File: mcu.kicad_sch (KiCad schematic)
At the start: 30 parts, among them J7 CONN_MCU_SERIAL, SW1 SW_RST, SW2 SW_BOOT0, U2 STM32F765IITx, Y2 25MHz

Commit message: Final annotate pass
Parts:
- gave numbers to parts that had none: 1
- renumbered C9 to C301, C10 to C302, C11 to C303, C12 to C304, C13 to C305, C14 to C306, C15 to C307, C16 to C308, C17 to C309, C18 to C310, C19 to C311, C20 to C312, C21 to C313, C22 to C314, C23 to C315, C24 to C316, C25 to C317, C26 to C318, C27 to C319, C28 to C320, J7 to J301, R12 to R301, R13 to R302, R14 to R303, R15 to R304, SW1 to SW301, SW2 to SW302, U2 to U301, Y2 to Y301

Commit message: Re-annotation, footprints
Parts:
- J301: footprint (none) -> Connector_PinSocket_2.54mm:PinSocket_1x05_P2.54mm_Vertical
- J302: footprint (none) -> Connector_PinSocket_2.54mm:PinSocket_1x13_P2.54mm_Vertical
- R301, R302, R303, R304: footprint (none) -> Resistor_SMD:R_0603_1608Metric_Pad0.98x0.95mm_HandSolder
- Y301: footprint Crystal:Crystal_SMD_5032-4Pin_5.0x3.2mm -> Crystal:Crystal_SMD_5032-2Pin_5.0x3.2mm_HandSoldering
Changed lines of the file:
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@@
       (effects (font (size 1.27 1.27)) (justify left))
     )
-    (property "Footprint" "" (id 2) (at 139.192 157.48 90)
+    (property "Footprint" "Resistor_SMD:R_0603_1608Metric_Pad0.98x0.95mm_HandSolder" (id 2) (at 139.192 157.48 90)
       (effects (font (size 1.27 1.27)) hide)
     )
@@
     (property "Reference" "R301" (id 0) (at 39.37 134.62 90))
     (property "Value" "10k" (id 1) (at 39.37 132.4411 90))
-    (property "Footprint" "" (id 2) (at 39.37 136.398 90)
+    (property "Footprint" "Resistor_SMD:R_0603_1608Metric_Pad0.98x0.95mm_HandSolder" (id 2) (at 39.37 136.398 90)
       (effects (font (size 1.27 1.27)) hide)
     )
@@
     (property "Reference" "R303" (id 0) (at 39.37 144.78 90))
     (property "Value" "10k" (id 1) (at 39.37 142.6011 90))
-    (property "Footprint" "" (id 2) (at 39.37 146.558 90)
+    (property "Footprint" "Resistor_SMD:R_0603_1608Metric_Pad0.98x0.95mm_HandSolder" (id 2) (at 39.37 146.558 90)
       (effects (font (size 1.27 1.27)) hide)
     )
@@
     (property "Reference" "R302" (id 0) (at 39.37 139.7 90))
     (property "Value" "10k" (id 1) (at 39.37 137.5211 90))
-    (property "Footprint" "" (id 2) (at 39.37 141.478 90)
+    (property "Footprint" "Resistor_SMD:R_0603_1608Metric_Pad0.98x0.95mm_HandSolder" (id 2) (at 39.37 141.478 90)
       (effects (font (size 1.27 1.27)) hide)
     )
@@
     (property "Reference" "J302" (id 0) (at 210.82 146.211 90))
     (property "Value" "Conn_01x13_Female" (id 1) (at 210.82 148.7479 90))
-    (property "Footprint" "" (id 2) (at 210.82 149.86 0)
+    (property "Footprint" "Connector_PinSocket_2.54mm:PinSocket_1x13_P2.54mm_Vertical" (id 2) (at 210.82 149.86 0)
       (effects (font (size 1.27 1.27)) hide)
     )
@@
       (effects (font (size 1.27 1.27)) (justify left))
     )
-    (property "Footprint" "Crystal:Crystal_SMD_5032-4Pin_5.0x3.2mm" (id 2) (at 139.7 171.45 0)
+    (property "Footprint" "Crystal:Crystal_SMD_5032-2Pin_5.0x3.2mm_HandSoldering" (id 2) (at 139.7 171.45 0)
       (effects (font (size 1.27 1.27)) hide)
     )
@@
     (property "Reference" "J301" (id 0) (at 104.14 155.101 90))
     (property "Value" "CONN_MCU_SERIAL" (id 1) (at 104.14 157.6379 90))
-    (property "Footprint" "" (id 2) (at 105.41 158.75 0)
-      (effects (font (size 1.27 1.27)) hide)
-    )
+    (property "Footprint" "Connector_PinSocket_2.54mm:PinSocket_1x05_P2.54mm_Vertical" (id 2) (at 105.41 158.75 0)
+      (effects (font (size 1.27 1.27)) hide)
+    )

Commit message: Add button footprint
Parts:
- SW301, SW302: footprint (none) -> marco-ram-board:DTSMW69N
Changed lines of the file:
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@@
       (effects (font (size 1.27 1.27)) (justify right))
     )
-    (property "Footprint" "" (id 2) (at 57.15 157.48 0)
+    (property "Footprint" "marco-ram-board:DTSMW69N" (id 2) (at 57.15 157.48 0)
       (effects (font (size 1.27 1.27)) hide)
     )
@@
       (effects (font (size 1.27 1.27)) (justify right))
     )
-    (property "Footprint" "" (id 2) (at 46.99 161.29 0)
-      (effects (font (size 1.27 1.27)) hide)
-    )
+    (property "Footprint" "marco-ram-board:DTSMW69N" (id 2) (at 46.99 161.29 0)
+      (effects (font (size 1.27 1.27)) hide)
+    )

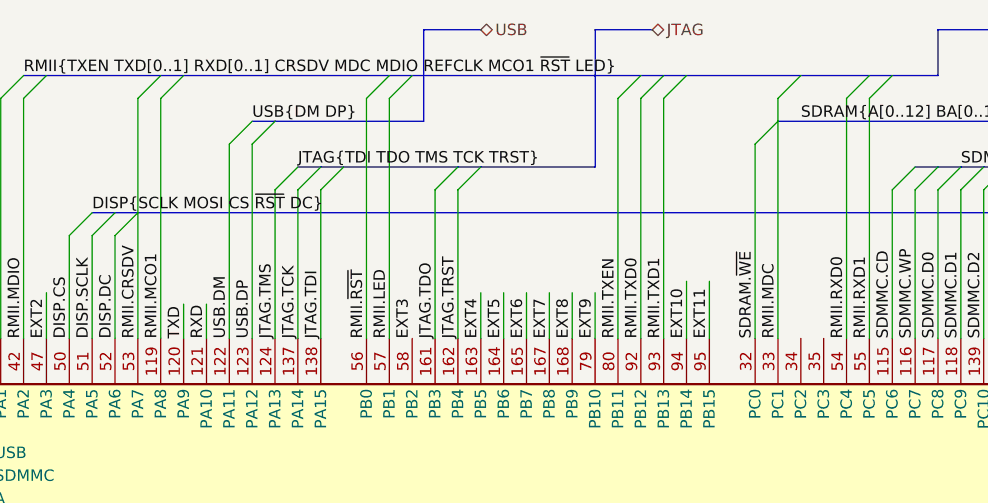
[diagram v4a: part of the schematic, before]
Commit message: Also connect MCU USB VBUS and ID.
Useful for detecting disconnections.
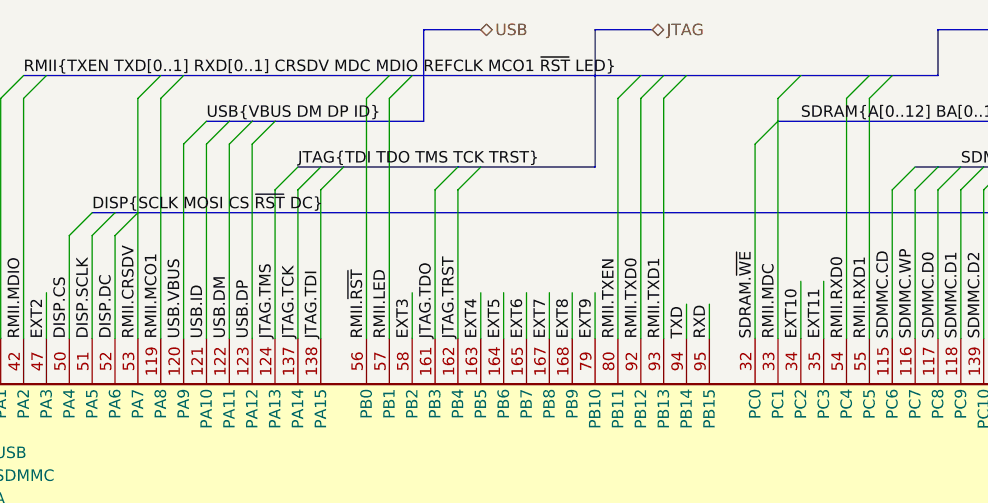
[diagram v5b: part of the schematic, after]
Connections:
- net EXT10: now also U301.34 (PC2); no longer U301.94 (PB14)
- net EXT11: now also U301.35 (PC3); no longer U301.95 (PB15)
- net RXD: now also U301.95 (PB15); no longer U301.121 (PA10)
- net TXD: now also U301.94 (PB14); no longer U301.120 (PA9)
- new net USB.ID: U301.121 (PA10)
- new net USB.VBUS: U301.120 (PA9)
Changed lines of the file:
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@@
+    (stroke (width 0) (type default) (color 0 0 0 0))
+  )
+  (bus_entry (at 80.01 26.67) (size -2.54 2.54)
     (stroke (width 0) (type default) (color 0 0 0 0))
   )
@@
     (stroke (width 0) (type default) (color 0 0 0 0))
   )
+  (bus_entry (at 77.47 26.67) (size -2.54 2.54)
+    (stroke (width 0) (type default) (color 0 0 0 0))
+  )
   (bus_entry (at 135.89 144.78) (size -2.54 -2.54)
     (stroke (width 0) (type default) (color 0 0 0 0))
@@
     (stroke (width 0) (type default) (color 0 0 0 0))
   )
-  (wire (pts (xy 130.81 44.45) (xy 130.81 50.8))
-    (stroke (width 0) (type default) (color 0 0 0 0))
-  )
   (wire (pts (xy 43.18 144.78) (xy 62.23 144.78))
     (stroke (width 0) (type default) (color 0 0 0 0))
@@
     (stroke (width 0) (type default) (color 0 0 0 0))
   )
+  (wire (pts (xy 130.81 46.99) (xy 130.81 50.8))
+    (stroke (width 0) (type default) (color 0 0 0 0))
+  )
   (wire (pts (xy 57.15 24.13) (xy 57.15 50.8))
     (stroke (width 0) (type default) (color 0 0 0 0))
@@
     (stroke (width 0) (type default) (color 0 0 0 0))
   )
+  (bus (pts (xy 82.55 26.67) (xy 85.09 26.67))
+    (stroke (width 0) (type default) (color 0 0 0 0))
+  )
   (wire (pts (xy 133.35 124.46) (xy 133.35 142.24))
     (stroke (width 0) (type default) (color 0 0 0 0))
@@
     (stroke (width 0) (type default) (color 0 0 0 0))
   )
+  (bus (pts (xy 77.47 26.67) (xy 80.01 26.67))
+    (stroke (width 0) (type default) (color 0 0 0 0))
+  )
   (wire (pts (xy 134.62 162.56) (xy 134.62 171.45))
     (stroke (width 0) (type default) (color 0 0 0 0))
@@
     (stroke (width 0) (type default) (color 0 0 0 0))
   )
-  (wire (pts (xy 133.35 44.45) (xy 133.35 50.8))
-    (stroke (width 0) (type default) (color 0 0 0 0))
-  )
   (wire (pts (xy 100.33 163.83) (xy 100.33 166.37))
     (stroke (width 0) (type default) (color 0 0 0 0))
@@
     (stroke (width 0) (type default) (color 0 0 0 0))
   )
+  (wire (pts (xy 146.05 44.45) (xy 146.05 50.8))
+    (stroke (width 0) (type default) (color 0 0 0 0))
+  )
+  (bus (pts (xy 80.01 26.67) (xy 82.55 26.67))
+    (stroke (width 0) (type default) (color 0 0 0 0))
+  )
   (wire (pts (xy 138.43 29.21) (xy 138.43 50.8))
     (stroke (width 0) (type default) (color 0 0 0 0))
@@
     (stroke (width 0) (type default) (color 0 0 0 0))
   )
-  (bus (pts (xy 82.55 26.67) (xy 85.09 26.67))
-    (stroke (width 0) (type default) (color 0 0 0 0))
-  )
   (bus (pts (xy 236.22 16.51) (xy 248.92 16.51))
     (stroke (width 0) (type default) (color 0 0 0 0))
@@
     (stroke (width 0) (type default) (color 0 0 0 0))
   )
+  (wire (pts (xy 74.93 29.21) (xy 74.93 50.8))
+    (stroke (width 0) (type default) (color 0 0 0 0))
+  )
   (wire (pts (xy 41.91 48.26) (xy 41.91 53.34))
     (stroke (width 0) (type default) (color 0 0 0 0))
   )
+  (wire (pts (xy 133.35 46.99) (xy 133.35 50.8))
+    (stroke (width 0) (type default) (color 0 0 0 0))
+  )
   (wire (pts (xy 232.41 124.46) (xy 232.41 137.16))
     (stroke (width 0) (type default) (color 0 0 0 0))
@@
     (stroke (width 0) (type default) (color 0 0 0 0))
   )
+  (wire (pts (xy 77.47 29.21) (xy 77.47 50.8))
+    (stroke (width 0) (type default) (color 0 0 0 0))
+  )
   (wire (pts (xy 41.91 83.82) (xy 41.91 86.36))
     (stroke (width 0) (type default) (color 0 0 0 0))
@@
     (stroke (width 0) (type default) (color 0 0 0 0))
   )
-  (wire (pts (xy 74.93 46.99) (xy 74.93 50.8))
-    (stroke (width 0) (type default) (color 0 0 0 0))
-  )
   (wire (pts (xy 274.32 83.82) (xy 274.32 86.36))
     (stroke (width 0) (type default) (color 0 0 0 0))
@@
     (stroke (width 0) (type default) (color 0 0 0 0))
   )
+  (wire (pts (xy 143.51 44.45) (xy 143.51 50.8))
+    (stroke (width 0) (type default) (color 0 0 0 0))
+  )
   (wire (pts (xy 219.71 29.21) (xy 219.71 50.8))
     (stroke (width 0) (type default) (color 0 0 0 0))
@@
     (stroke (width 0) (type default) (color 0 0 0 0))
   )
+  (wire (pts (xy 100.33 45.72) (xy 100.33 50.8))
+    (stroke (width 0) (type default) (color 0 0 0 0))
+  )
   (wire (pts (xy 67.31 39.37) (xy 67.31 50.8))
     (stroke (width 0) (type default) (color 0 0 0 0))
@@
     (stroke (width 0) (type default) (color 0 0 0 0))
   )
-  (wire (pts (xy 77.47 46.99) (xy 77.47 50.8))
-    (stroke (width 0) (type default) (color 0 0 0 0))
-  )
   (wire (pts (xy 146.05 124.46) (xy 146.05 137.16))
     (stroke (width 0) (type default) (color 0 0 0 0))
@@
     (effects (font (size 1.27 1.27)) (justify left bottom))
   )
-  (label "RXD" (at 77.47 50.8 90)
-    (effects (font (size 1.27 1.27)) (justify left bottom))
-  )
   (label "SDRAM.A4" (at 234.95 124.46 270)
     (effects (font (size 1.27 1.27)) (justify right bottom))
   )
-  (label "EXT11" (at 133.35 50.8 90)
+  (label "RXD" (at 133.35 50.8 90)
     (effects (font (size 1.27 1.27)) (justify left bottom))
   )
@@
     (effects (font (size 1.27 1.27)) (justify right bottom))
   )
+  (label "USB.ID" (at 77.47 50.8 90)
+    (effects (font (size 1.27 1.27)) (justify left bottom))
+  )
   (label "SDRAM.~{RAS}" (at 252.73 124.46 270)
     (effects (font (size 1.27 1.27)) (justify right bottom))
@@
     (effects (font (size 1.27 1.27)) (justify left bottom))
   )
-  (label "USB{DM DP}" (at 82.55 26.67 0)
+  (label "USB{VBUS DM DP ID}" (at 77.47 26.67 0)
     (effects (font (size 1.27 1.27)) (justify left bottom))
   )
@@
     (effects (font (size 1.27 1.27)) (justify right bottom))
   )
+  (label "EXT11" (at 146.05 50.8 90)
+    (effects (font (size 1.27 1.27)) (justify left bottom))
+  )
   (label "BTN[0..3]" (at 252.73 144.78 0)
     (effects (font (size 1.27 1.27)) (justify left bottom))
@@
     (effects (font (size 1.27 1.27)) (justify left bottom))
   )
-  (label "TXD" (at 74.93 50.8 90)
-    (effects (font (size 1.27 1.27)) (justify left bottom))
-  )
   (label "EXT3" (at 203.2 154.94 270)
     (effects (font (size 1.27 1.27)) (justify right bottom))
@@
     (effects (font (size 1.27 1.27)) (justify right bottom))
   )
+  (label "USB.VBUS" (at 74.93 50.8 90)
+    (effects (font (size 1.27 1.27)) (justify left bottom))
+  )
   (label "EXT7" (at 115.57 50.8 90)
     (effects (font (size 1.27 1.27)) (justify left bottom))
@@
     (effects (font (size 1.27 1.27)) (justify right bottom))
   )
-  (label "EXT10" (at 130.81 50.8 90)
+  (label "TXD" (at 130.81 50.8 90)
     (effects (font (size 1.27 1.27)) (justify left bottom))
   )
@@
     (effects (font (size 1.27 1.27)) (justify right bottom))
   )
+  (label "EXT10" (at 143.51 50.8 90)
+    (effects (font (size 1.27 1.27)) (justify left bottom))
+  )
   (label "SDRAM.D6" (at 247.65 50.8 90)

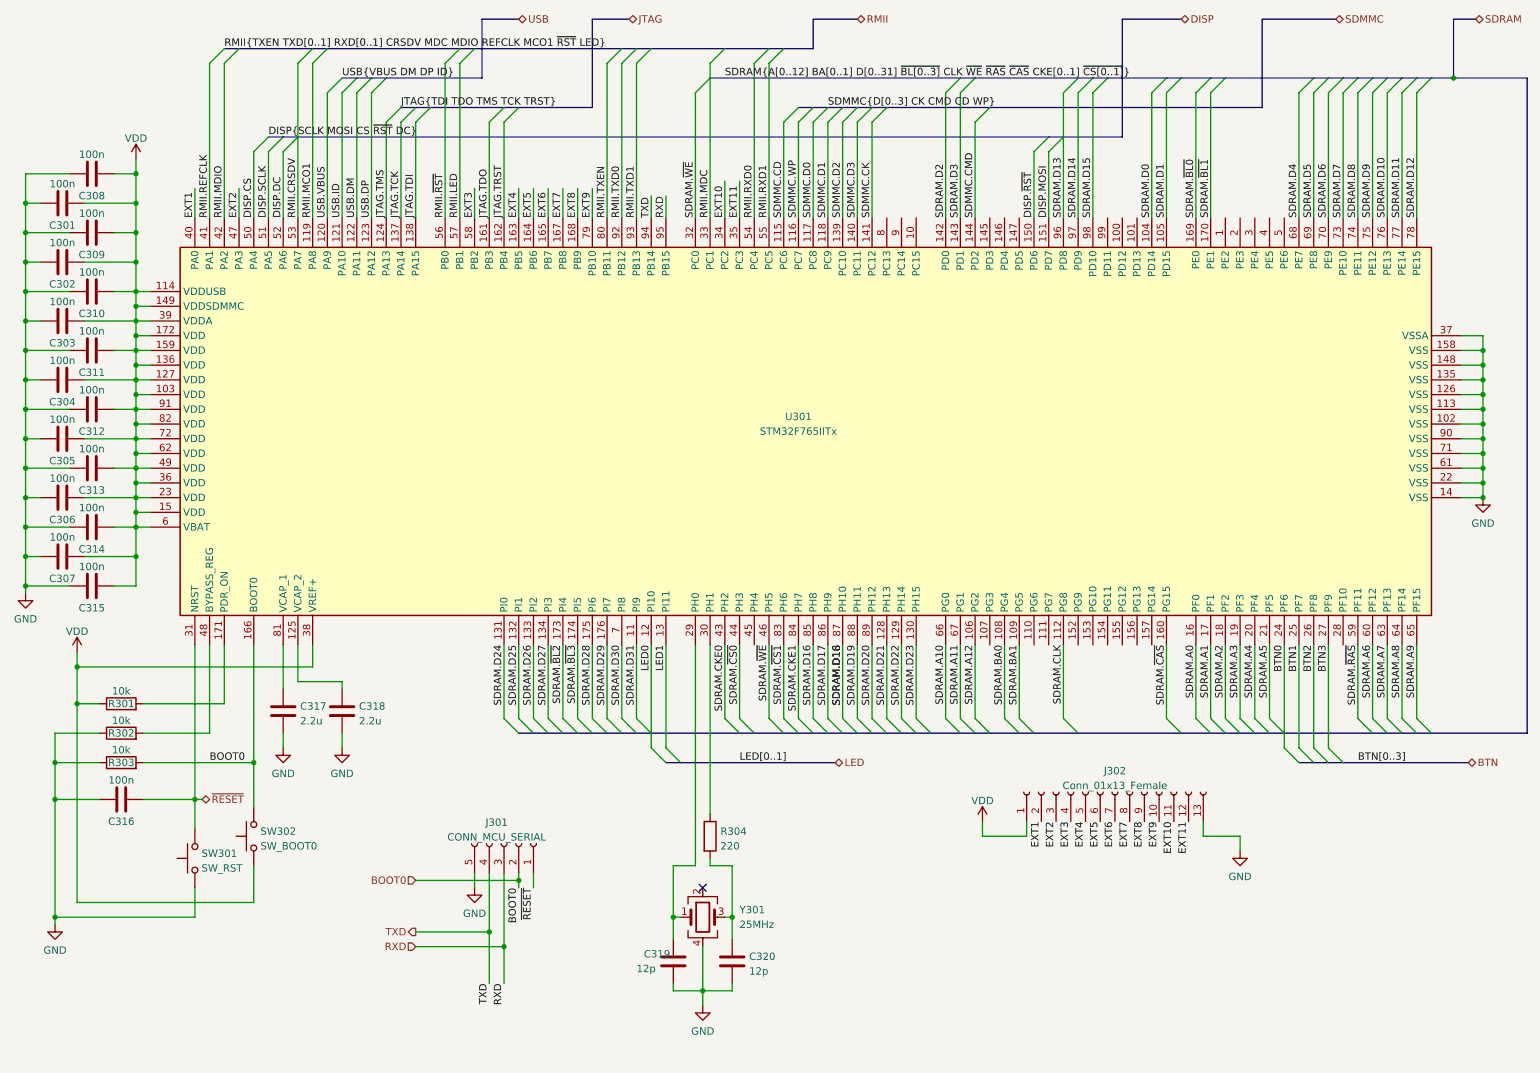
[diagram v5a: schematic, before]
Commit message: Move programming USART to USART3 from USART1 because the pins configured by the bootloader on USART1 are now occupied.
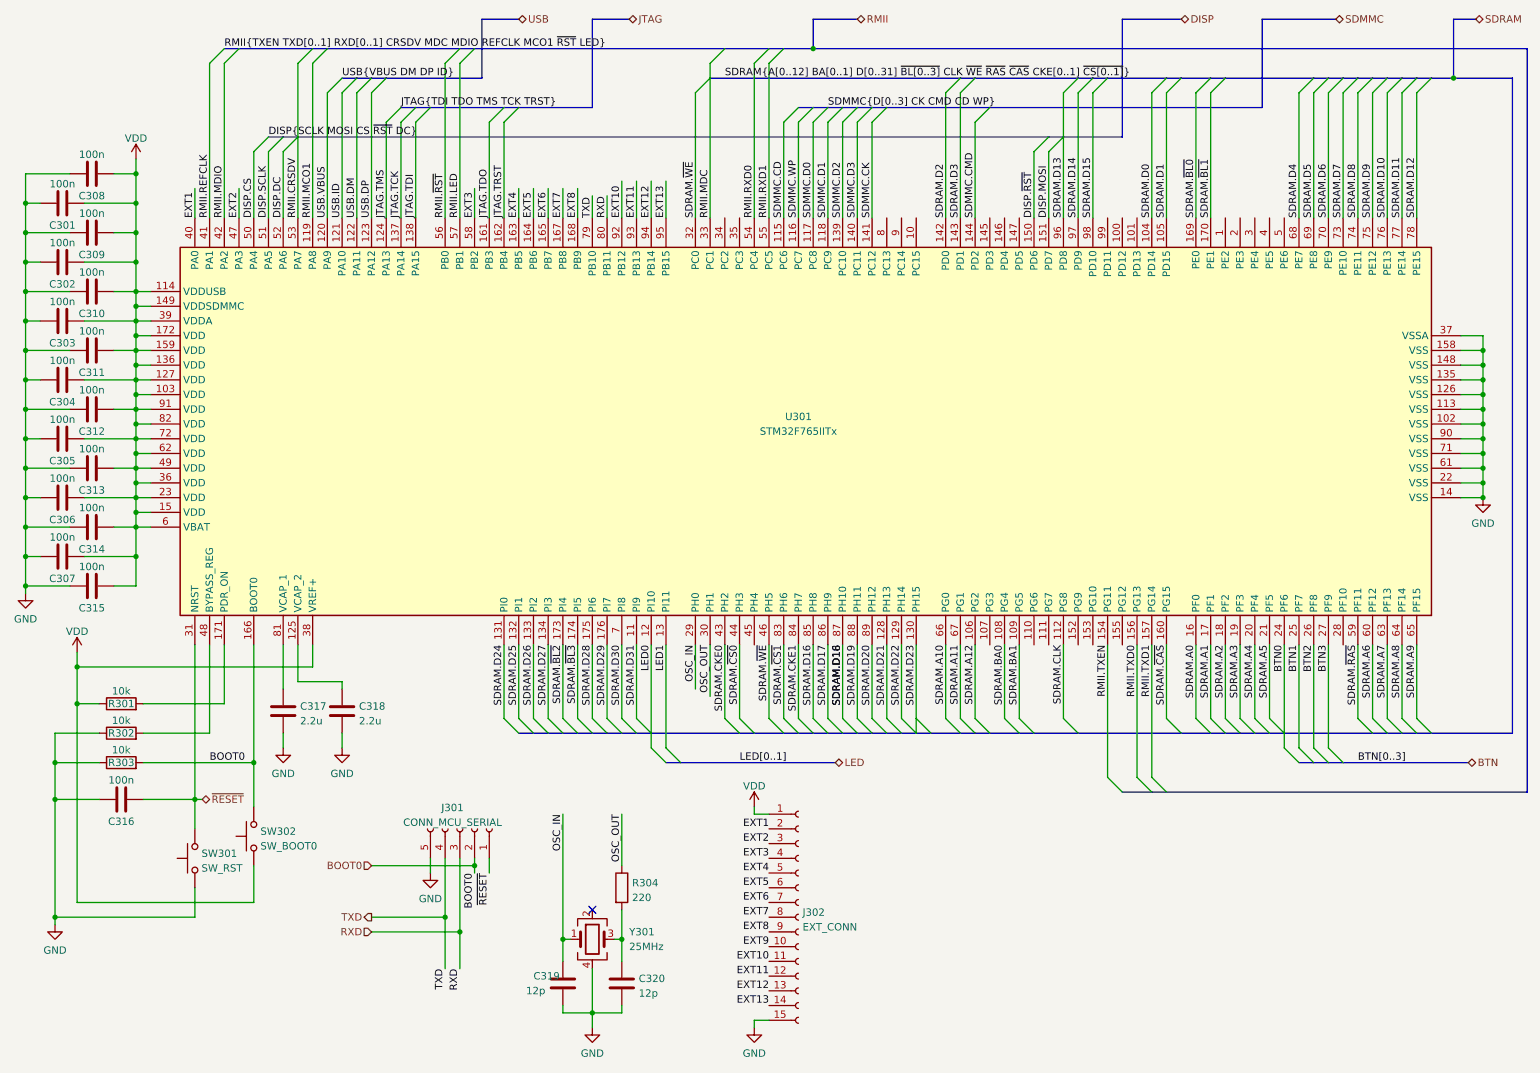
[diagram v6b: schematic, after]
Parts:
- removed J302: Conn_01x13_Female, Connector_PinSocket_2.54mm:PinSocket_1x13_P2.54mm_Vertical, symbol Connector:Conn_01x13_Female
- added J302: EXT_CONN, Connector_PinSocket_2.54mm:PinSocket_1x15_P2.54mm_Vertical, symbol Connector:Conn_01x15_Female
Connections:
- net EXT1: now also J302.2 (Pin_2)
- net EXT10: now also U301.92 (PB12), J302.11 (Pin_11); no longer U301.34 (PC2)
- net EXT11: now also U301.93 (PB13), J302.12 (Pin_12); no longer U301.35 (PC3)
- net EXT2: now also J302.3 (Pin_3)
- net EXT3: now also J302.4 (Pin_4)
- net EXT4: now also J302.5 (Pin_5)
- net EXT5: now also J302.6 (Pin_6)
- net EXT6: now also J302.7 (Pin_7)
- net EXT7: now also J302.8 (Pin_8)
- net EXT8: now also J302.9 (Pin_9)
- net EXT9: now also J302.10 (Pin_10); no longer U301.79 (PB10)
- net GND: now also J302.15 (Pin_15)
- net RMII.TXD0: now also U301.156 (PG13); no longer U301.92 (PB12)
- net RMII.TXD1: now also U301.157 (PG14); no longer U301.93 (PB13)
- net RMII.TXEN: now also U301.154 (PG11); no longer U301.80 (PB11)
- net RXD: now also U301.80 (PB11); no longer U301.95 (PB15)
- net TXD: now also U301.79 (PB10); no longer U301.94 (PB14)
- net VDD: now also J302.1 (Pin_1)
- net OSC_OUT: now reaches R304.1, U301.30 (PH1)
- net OSC_IN: now reaches C319.1, U301.29 (PH0), Y301.1
- new net EXT12: J302.13 (Pin_13), U301.94 (PB14)
- new net EXT13: J302.14 (Pin_14), U301.95 (PB15)
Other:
- moved on the sheet: C319, C320, J301, R304, Y301

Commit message: Placement almost complete
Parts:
- Y301: footprint Crystal:Crystal_SMD_5032-2Pin_5.0x3.2mm_HandSoldering -> Crystal:Crystal_SMD_5032-4Pin_5.0x3.2mm
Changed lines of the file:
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@@
       (effects (font (size 1.27 1.27)) (justify left))
     )
-    (property "Footprint" "Crystal:Crystal_SMD_5032-2Pin_5.0x3.2mm_HandSoldering" (id 2) (at 120.65 175.26 0)
+    (property "Footprint" "Crystal:Crystal_SMD_5032-4Pin_5.0x3.2mm" (id 2) (at 120.65 175.26 0)
       (effects (font (size 1.27 1.27)) hide)
     )
